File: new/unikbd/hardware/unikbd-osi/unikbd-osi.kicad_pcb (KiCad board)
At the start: 2 copper layers, 76.2 x 114.3 mm, 13 parts, among them J1 Conn_01x16, J2 Conn_02x20_Odd_Even, U1 7402, U2 74LS240, U3 74LS240, U4 74LS373

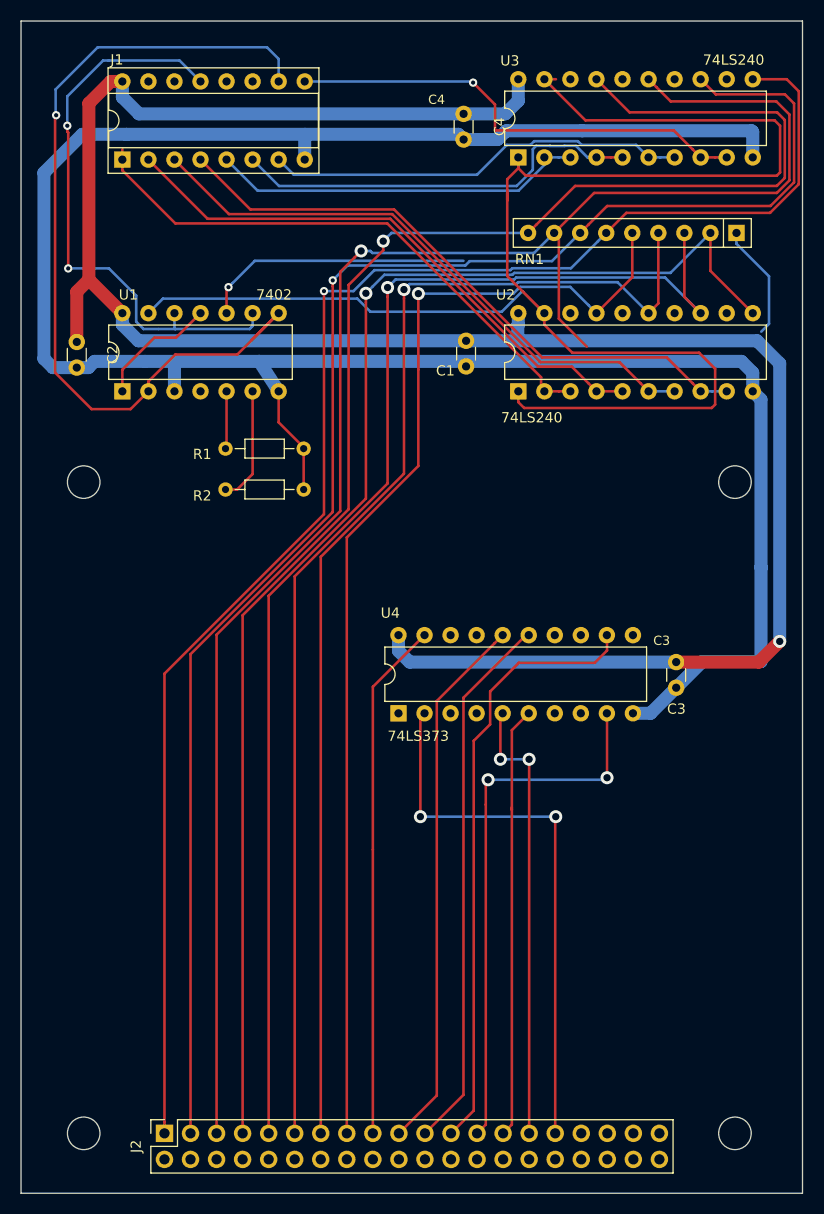
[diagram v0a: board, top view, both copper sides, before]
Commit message: update 502 files to fix missing traces
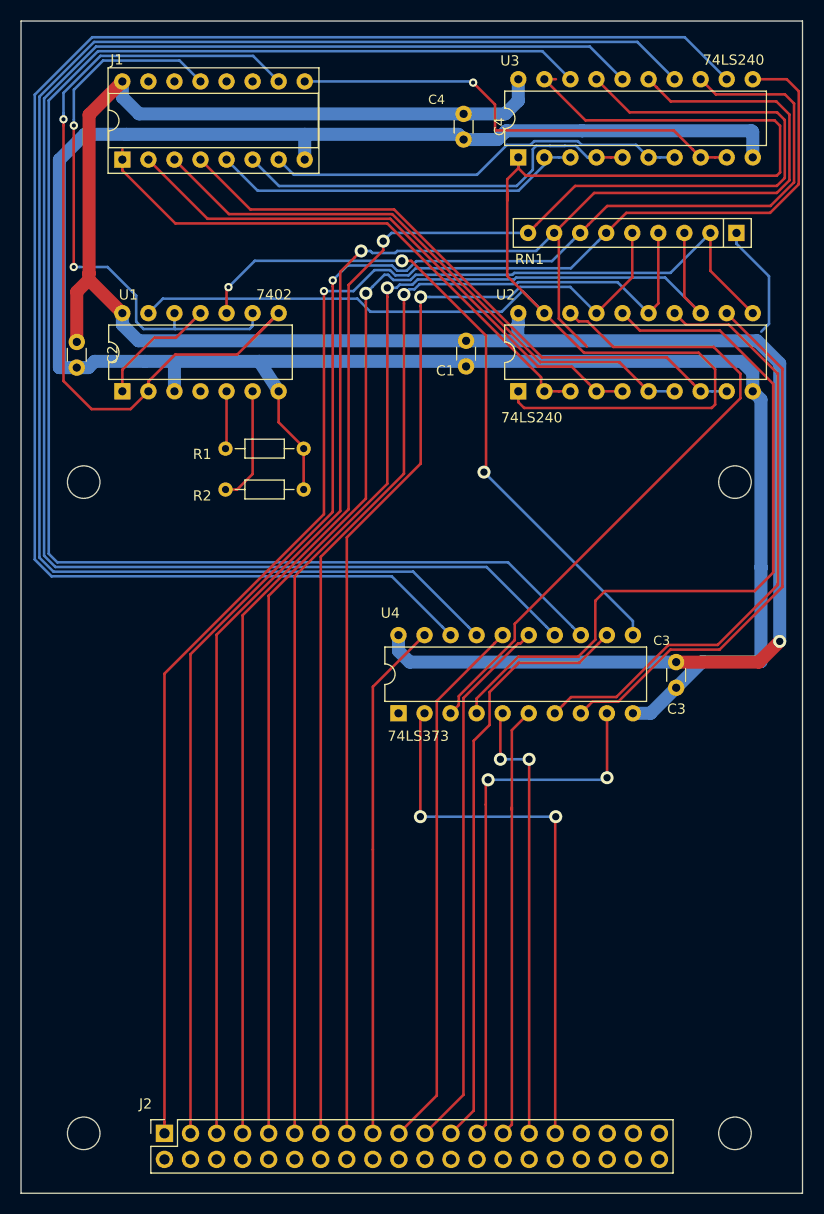
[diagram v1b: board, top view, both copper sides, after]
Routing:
- net Net-(U3-Pad12): track 0.00 -> 160.4 mm
- net Net-(U3-Pad16): track 0.00 -> 157.4 mm
- net Net-(U3-Pad14): track 0.00 -> 156.4 mm
- net Net-(U3-Pad18): track 0.00 -> 153.4 mm
- net Net-(U2-Pad16): track 0.00 -> 73.6 mm
- net Net-(U2-Pad18): track 0.00 -> 63.8 mm
- net Net-(U2-Pad14): track 0.00 -> 60.0 mm
- net Net-(U2-Pad12): track 0.00 -> 53.7 mm
- net Net-(U1-Pad10): track 26.6 -> 67.1 mm, vias 1 -> 3
- net /R_~W: track 85.2 -> 81.9 mm
- net GND: track 224.8 -> 223.0 mm
- net /~KBE: track 57.5 -> 56.6 mm
- net /Row4: track 59.2 -> 58.3 mm
- net Net-(U1-Pad13): track 160.5 -> 159.8 mm
- net +5V: track 224.7 -> 224.0 mm
